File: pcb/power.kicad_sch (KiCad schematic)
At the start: 42 parts, among them J4 Conn_01x02_Socket, J5 Conn_01x03_Socket, U3 TPS63802DLAR, U4 BQ24078RGTR, U6 SN74LVC1G79DBVT

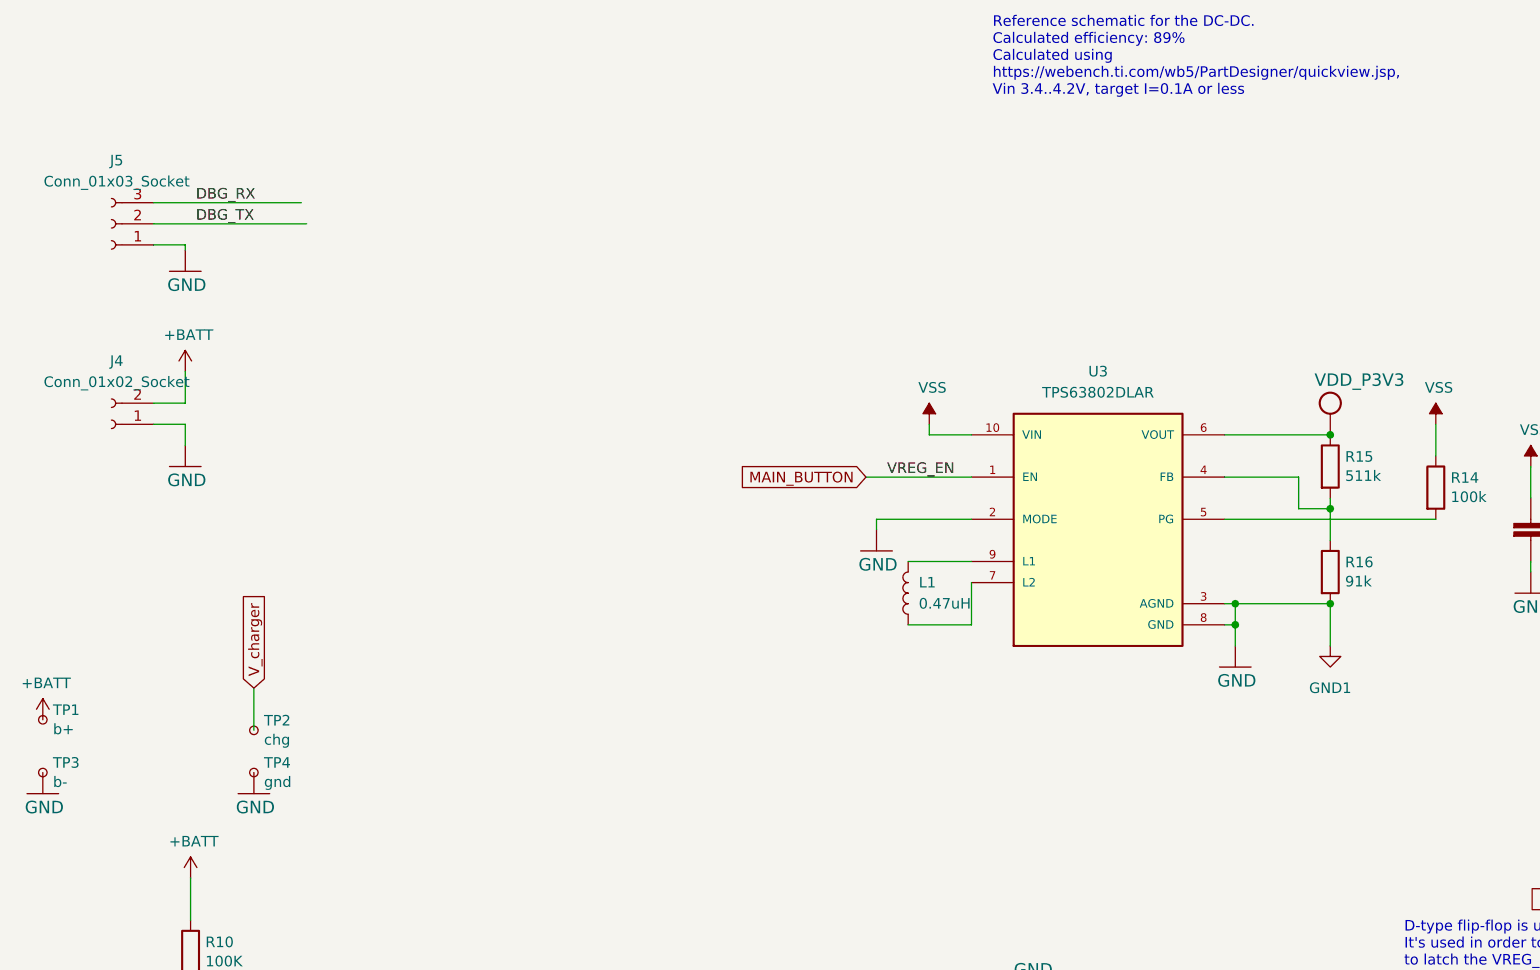
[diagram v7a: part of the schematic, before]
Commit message: saving changes: layout looks good, most DRC errors are fixed
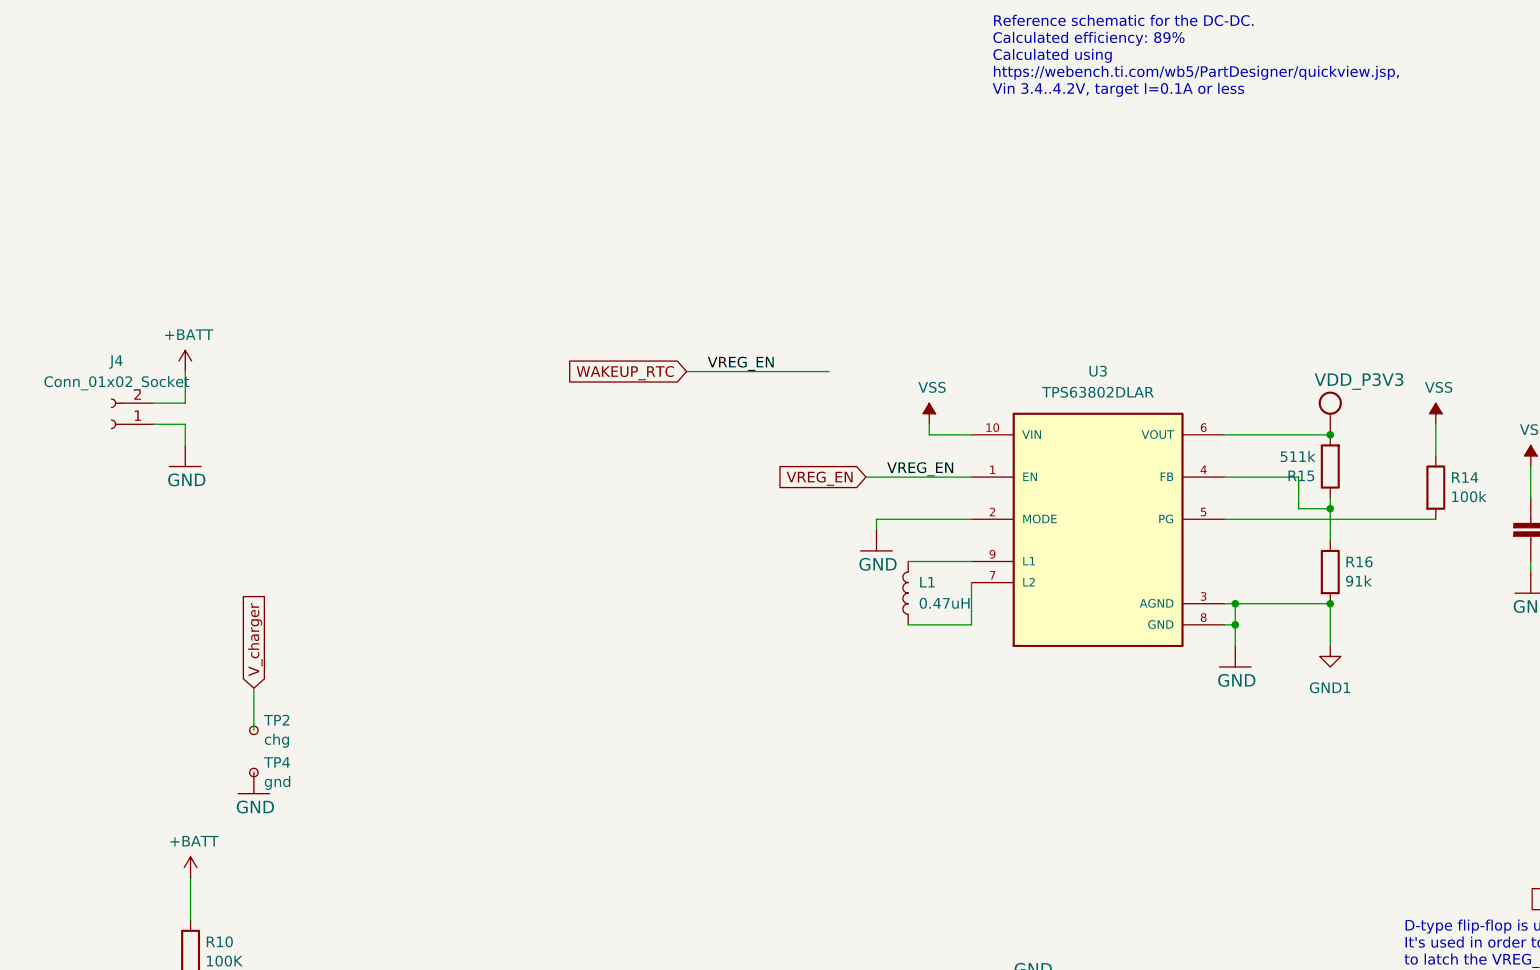
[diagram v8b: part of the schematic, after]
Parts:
- removed J5: Conn_01x03_Socket, _other:JST_SM03B-SRSS-TB_LF__SN_, symbol Connector:Conn_01x03_Socket
- removed TP1: b+, TestPoint:TestPoint_Pad_D1.0mm, symbol Connector:TestPoint_Small
- removed TP3: b-, TestPoint:TestPoint_Pad_D1.0mm, symbol Connector:TestPoint_Small
- R15: footprint Resistor_SMD:R_0402_1005Metric -> Resistor_SMD:R_0603_1608Metric; LCSC C144750 -> C188257
- R16: footprint Resistor_SMD:R_0402_1005Metric -> Resistor_SMD:R_0603_1608Metric; LCSC C4190 -> C227535
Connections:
- net VCC: now also R15.2; no longer R15.1
- net at R16.1, U3.4 (FB): now also R15.1; no longer R15.2
- net MAIN_BUTTON renamed VREG_EN
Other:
- moved on the sheet: R15
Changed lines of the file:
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@@
 (kicad_sch (version 20230121) (generator eeschema)
   (paper "A4")
+  (junction (at 162.56 67.31) (diameter 0) (color 0 0 0 0)
+  )
   (junction (at 276.86 120.65) (diameter 0) (color 0 0 0 0)
   )
@@
   (junction (at 129.54 152.4) (diameter 0) (color 0 0 0 0)
   )
-  (junction (at 162.56 67.31) (diameter 0) (color 0 0 0 0)
-  )
   (junction (at 151.13 87.63) (diameter 0) (color 0 0 0 0)
   )
@@
   )
   (no_connect (at 74.93 162.56))
-  (wire (pts (xy 20.955 44.45) (xy 24.765 44.45))
-    (stroke (width 0) (type default))
-  )
   (wire (pts (xy 125.73 154.94) (xy 129.54 154.94))
     (stroke (width 0) (type default))
@@
     (stroke (width 0) (type default))
   )
-  (wire (pts (xy 20.955 41.91) (xy 39.37 41.91))
+  (wire (pts (xy 85.09 59.69) (xy 102.235 59.69))
     (stroke (width 0) (type default))
   )
@@
     (stroke (width 0) (type default))
   )
-  (wire (pts (xy 24.765 44.45) (xy 24.765 45.085))
-    (stroke (width 0) (type default))
-  )
   (wire (pts (xy 114.3 67.31) (xy 119.38 67.31))
     (stroke (width 0) (type default))
@@
   )
   (wire (pts (xy 227.33 120.65) (xy 234.95 120.65))
-    (stroke (width 0) (type default))
-  )
-  (wire (pts (xy 20.955 39.37) (xy 38.735 39.37))
     (stroke (width 0) (type default))
   )
@@
     (effects (font (size 1.27 1.27)) (justify left bottom))
   )
-  (label "DBG_RX" (at 26.035 39.37 0) (fields_autoplaced)
+  (label "VREG_EN" (at 87.63 59.69 0) (fields_autoplaced)
     (effects (font (size 1.27 1.27)) (justify left bottom))
   )
   (label "FF_CLK" (at 209.55 154.94 0) (fields_autoplaced)
-    (effects (font (size 1.27 1.27)) (justify left bottom))
-  )
-  (label "DBG_TX" (at 26.035 41.91 0) (fields_autoplaced)
     (effects (font (size 1.27 1.27)) (justify left bottom))
   )
@@
     )
   )
-  (global_label "MAIN_BUTTON" (shape input) (at 106.68 72.39 180) (fields_autoplaced)
+  (global_label "WAKEUP_RTC" (shape input) (at 85.09 59.69 180) (fields_autoplaced)
     (effects (font (size 1.27 1.27)) (justify right))
-    (property "Intersheetrefs" "${INTERSHEET_REFS}" (at -43.18 29.21 0)
-      (effects (font (size 1.27 1.27)) hide)
+    (property "Intersheetrefs" "${INTERSHEET_REFS}" (at 70.7243 59.69 0)
+      (effects (font (size 1.27 1.27)) (justify right) hide)
+    )
+  )
+  (global_label "VREG_EN" (shape input) (at 106.68 72.39 180) (fields_autoplaced)
+    (effects (font (size 1.27 1.27)) (justify right))
+    (property "Intersheetrefs" "${INTERSHEET_REFS}" (at 96.1243 72.39 0)
+      (effects (font (size 1.27 1.27)) (justify right) hide)
     )
   )
@@
     )
   )
-  (symbol (lib_id "power:+BATT") (at 7.62 101.6 0) (unit 1)
-    (in_bom yes) (on_board yes) (dnp no)
-    (property "Reference" "#PWR05" (at 7.62 105.41 0)
-      (effects (font (size 1.27 1.27)) hide)
-    )
-    (property "Value" "+BATT" (at 8.001 97.2058 0)
-      (effects (font (size 1.27 1.27)))
-    )
-    (property "Footprint" "" (at 7.62 101.6 0)
-      (effects (font (size 1.27 1.27)) hide)
-    )
-    (property "Datasheet" "" (at 7.62 101.6 0)
-      (effects (font (size 1.27 1.27)) hide)
-    )
-    (pin "1")
-    (instances
-      (project "nRF52832_qfaa"
-        (path "/109caac1-5036-4f23-9a66-f569d871501b/00000000-0000-0000-0000-000061764c1f"
-          (reference "#PWR05") (unit 1)
-        )
-      )
-    )
-  )
-  (symbol (lib_id "nRF52832_qfaa-eagle-import:GND") (at 7.62 110.49 0) (mirror y) (unit 1)
-    (in_bom yes) (on_board yes) (dnp no)
-    (property "Reference" "#GND025" (at 7.62 110.49 0)
-      (effects (font (size 1.27 1.27)) hide)
-    )
-    (property "Value" "GND" (at 10.16 113.03 0)
-      (effects (font (size 1.4986 1.4986)) (justify left bottom))
-    )
-    (property "Footprint" "" (at 7.62 110.49 0)
-      (effects (font (size 1.27 1.27)) hide)
-    )
-    (property "Datasheet" "" (at 7.62 110.49 0)
-      (effects (font (size 1.27 1.27)) hide)
-    )
-    (pin "1")
-    (instances
-      (project "nRF52832_qfaa"
-        (path "/109caac1-5036-4f23-9a66-f569d871501b/00000000-0000-0000-0000-000061764c1f"
-          (reference "#GND025") (unit 1)
-        )
-      )
-    )
-  )
   (symbol (lib_id "Device:R") (at 127 139.7 0) (unit 1)
     (in_bom yes) (on_board yes) (dnp no)
@@
         (path "/109caac1-5036-4f23-9a66-f569d871501b/00000000-0000-0000-0000-000061764c1f"
           (reference "TP4") (unit 1)
-        )
-      )
-    )
-  )
-  (symbol (lib_id "Connector:TestPoint_Small") (at 7.62 107.95 0) (unit 1)
-    (in_bom yes) (on_board yes) (dnp no)
-    (property "Reference" "TP3" (at 8.8392 106.7816 0)
-      (effects (font (size 1.27 1.27)) (justify left))
-    )
-    (property "Value" "b-" (at 8.8392 109.093 0)
-      (effects (font (size 1.27 1.27)) (justify left))
-    )
-    (property "Footprint" "TestPoint:TestPoint_Pad_D1.0mm" (at 12.7 107.95 0)
-      (effects (font (size 1.27 1.27)) hide)
-    )
-    (property "Datasheet" "~" (at 12.7 107.95 0)
-      (effects (font (size 1.27 1.27)) hide)
-    )
-    (pin "1")
-    (instances
-      (project "nRF52832_qfaa"
-        (path "/109caac1-5036-4f23-9a66-f569d871501b/00000000-0000-0000-0000-000061764c1f"
-          (reference "TP3") (unit 1)
-        )
-      )
-    )
-  )
-  (symbol (lib_id "Connector:TestPoint_Small") (at 7.62 101.6 0) (unit 1)
-    (in_bom yes) (on_board yes) (dnp no)
-    (property "Reference" "TP1" (at 8.8392 100.4316 0)
-      (effects (font (size 1.27 1.27)) (justify left))
-    )
-    (property "Value" "b+" (at 8.8392 102.743 0)
-      (effects (font (size 1.27 1.27)) (justify left))
-    )
-    (property "Footprint" "TestPoint:TestPoint_Pad_D1.0mm" (at 12.7 101.6 0)
-      (effects (font (size 1.27 1.27)) hide)
-    )
-    (property "Datasheet" "~" (at 12.7 101.6 0)
-      (effects (font (size 1.27 1.27)) hide)
-    )
-    (pin "1")
-    (instances
-      (project "nRF52832_qfaa"
-        (path "/109caac1-5036-4f23-9a66-f569d871501b/00000000-0000-0000-0000-000061764c1f"
-          (reference "TP1") (unit 1)
         )
       )
@@
     )
   )
-  (symbol (lib_id "Connector:Conn_01x03_Socket") (at 15.875 41.91 180) (unit 1)
-    (in_bom yes) (on_board yes) (dnp no) (fields_autoplaced)
-    (property "Reference" "J5" (at 16.51 34.29 0)
-      (effects (font (size 1.27 1.27)))
-    )
-    (property "Value" "Conn_01x03_Socket" (at 16.51 36.83 0)
-      (effects (font (size 1.27 1.27)))
-    )
-    (property "Footprint" "_other:JST_SM03B-SRSS-TB_LF__SN_" (at 15.875 41.91 0)
-      (effects (font (size 1.27 1.27)) hide)
-    )
-    (property "Datasheet" "~" (at 15.875 41.91 0)
-      (effects (font (size 1.27 1.27)) hide)
-    )
-    (property "Populate" "" (at 15.875 41.91 0)
-      (effects (font (size 1.27 1.27)) hide)
-    )
-    (pin "2")
-    (pin "1")
-    (pin "3")
-    (instances
-      (project "nRF52832_qfaa"
-        (path "/109caac1-5036-4f23-9a66-f569d871501b/00000000-0000-0000-0000-000061764c1f"
-          (reference "J5") (unit 1)
-        )
-      )
-    )
-  )
   (symbol (lib_id "Connector:TestPoint") (at 227.33 55.88 0) (unit 1)
     (in_bom yes) (on_board yes) (dnp no)
@@
     )
   )
-  (symbol (lib_id "Device:R") (at 162.56 71.12 0) (unit 1)
-    (in_bom yes) (on_board yes) (dnp no)
-    (property "Reference" "R15" (at 164.338 69.9516 0)
-      (effects (font (size 1.27 1.27)) (justify left))
-    )
-    (property "Value" "511k" (at 164.338 72.263 0)
-      (effects (font (size 1.27 1.27)) (justify left))
-    )
-    (property "Footprint" "Resistor_SMD:R_0402_1005Metric" (at 160.782 71.12 90)
+  (symbol (lib_id "Device:R") (at 162.56 71.12 180) (unit 1)
+    (in_bom yes) (on_board yes) (dnp no)
+    (property "Reference" "R15" (at 160.782 72.2884 0)
+      (effects (font (size 1.27 1.27)) (justify left))
+    )
+    (property "Value" "511k" (at 160.782 69.977 0)
+      (effects (font (size 1.27 1.27)) (justify left))
+    )
+    (property "Footprint" "Resistor_SMD:R_0603_1608Metric" (at 164.338 71.12 90)
       (effects (font (size 1.27 1.27)) hide)
     )
@@
       (effects (font (size 1.27 1.27)) hide)
     )
-    (property "LCSC" "C144750" (at 162.56 71.12 0)
+    (property "LCSC" "C188257" (at 162.56 71.12 0)
+      (effects (font (size 1.27 1.27)) hide)
+    )
+    (property "Populate" "" (at 162.56 71.12 0)
       (effects (font (size 1.27 1.27)) hide)
     )
@@
       (effects (font (size 1.27 1.27)) (justify left))
     )
-    (property "Footprint" "Resistor_SMD:R_0402_1005Metric" (at 160.782 83.82 90)
+    (property "Footprint" "Resistor_SMD:R_0603_1608Metric" (at 160.782 83.82 90)
       (effects (font (size 1.27 1.27)) hide)
     )
@@
       (effects (font (size 1.27 1.27)) hide)
     )
-    (property "LCSC" "C4190" (at 162.56 83.82 0)
+    (property "LCSC" "C227535" (at 162.56 83.82 0)
+      (effects (font (size 1.27 1.27)) hide)
+    )
+    (property "Populate" "" (at 162.56 83.82 0)
       (effects (font (size 1.27 1.27)) hide)
     )
@@
         )
       )
-    )
-  )
-  (symbol (lib_id "nRF52832_qfaa-eagle-import:GND") (at 24.765 47.625 0) (mirror y) (unit 1)
-    (in_bom yes) (on_board yes) (dnp no)
-    (property "Reference" "#GND05" (at 24.765 47.625 0)
-      (effects (font (size 1.27 1.27)) hide)
-    )
-    (property "Value" "GND" (at 27.305 50.165 0)
-      (effects (font (size 1.4986 1.4986)) (justify left bottom))
-    )
-    (property "Footprint" "" (at 24.765 47.625 0)
-      (effects (font (size 1.27 1.27)) hide)
-    )
-    (property "Datasheet" "" (at 24.765 47.625 0)
-      (effects (font (size 1.27 1.27)) hide)
-    )
-    (pin "1")
-    (instances
-      (project "nRF52832_qfaa"
-        (path "/109caac1-5036-4f23-9a66-f569d871501b/00000000-0000-0000-0000-000061764c1f"
-          (reference "#GND05") (unit 1)
-        )
-      )
